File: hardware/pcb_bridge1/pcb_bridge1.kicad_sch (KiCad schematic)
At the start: 1 part, among them J1 TSM-103-01-L-DH

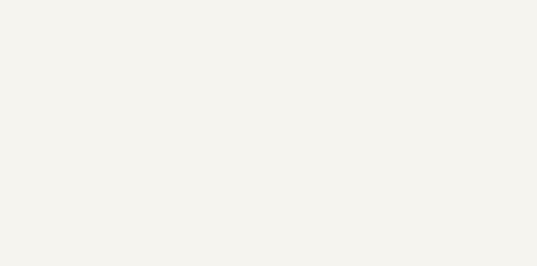
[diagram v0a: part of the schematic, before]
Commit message: Battery, zif added
nrf test points reduced
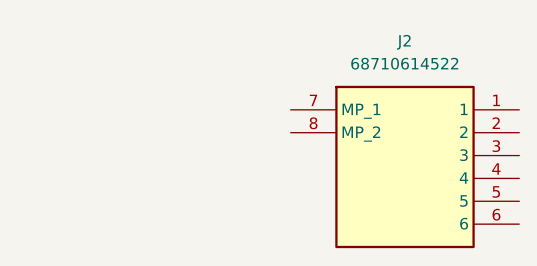
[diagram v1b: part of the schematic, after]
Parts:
- added J2: 68710614522, foots:68710614522, symbol 68710614522:68710614522
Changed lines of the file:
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@@
 	(paper "A4")
+	(symbol
+		(lib_id "68710614522:68710614522")
+		(at 128.27 43.18 0)
+		(unit 1)
+		(exclude_from_sim no)
+		(in_bom yes)
+		(on_board yes)
+		(dnp no)
+		(fields_autoplaced yes)
+		(property "Reference" "J2"
+			(at 140.97 35.56 0)
+			(effects
+				(font
+					(size 1.27 1.27)
+				)
+			)
+		)
+		(property "Value" "68710614522"
+			(at 140.97 38.1 0)
+			(effects
+				(font
+					(size 1.27 1.27)
+				)
+			)
+		)
+		(property "Footprint" "foots:68710614522"
+			(at 149.86 138.1 0)
+			(effects
+				(font
+					(size 1.27 1.27)
+				)
+				(justify left top)
+				(hide yes)
+			)
+		)
+		(property "Datasheet" ""
+			(at 149.86 238.1 0)
+			(effects
+				(font
+					(size 1.27 1.27)
+				)
+				(justify left top)
+				(hide yes)
+			)
+		)
+		(property "Description" "25WR-FPC 0.5mm ZIF Connector Bottom 6pin Wurth Elektronik 687 Series 0.5mm 6 Way 1 Row Straight PCB Socket Surface Mount Wire to Board"
+			(at 128.27 43.18 0)
+			(effects
+				(font
+					(size 1.27 1.27)
+				)
+				(hide yes)
+			)
+		)
+		(property "Height" "2.25"
+			(at 149.86 438.1 0)
+			(effects
+				(font
+					(size 1.27 1.27)
+				)
+				(justify left top)
+				(hide yes)
+			)
+		)
+		(property "Mouser Part Number" "710-68710614522"
+			(at 149.86 538.1 0)
+			(effects
+				(font
+					(size 1.27 1.27)
+				)
+				(justify left top)
+				(hide yes)
+			)
+		)
+		(property "Mouser Price/Stock" "https://www.mouser.co.uk/ProductDetail/Wurth-Elektronik/68710614522?qs=ZtY9WdtwX56jW0fVCAMn0A%3D%3D"
+			(at 149.86 638.1 0)
+			(effects
+				(font
+					(size 1.27 1.27)
+				)
+				(justify left top)
+				(hide yes)
+			)
+		)
+		(property "Manufacturer_Name" "Wurth Elektronik"
+			(at 149.86 738.1 0)
+			(effects
+				(font
+					(size 1.27 1.27)
+				)
+				(justify left top)
+				(hide yes)
+			)
+		)
+		(property "Manufacturer_Part_Number" "68710614522"
+			(at 149.86 838.1 0)
+			(effects
+				(font
+					(size 1.27 1.27)
+				)
+				(justify left top)
+				(hide yes)
+			)
+		)
+		(property "Distributor Link" "https://www.mouser.co.uk/ProductDetail/Wurth-Elektronik/68710614522?qs=ZtY9WdtwX56jW0fVCAMn0A%3D%3D"
+			(at 128.27 43.18 0)
+			(effects
+				(font
+					(size 1.27 1.27)
+				)
+				(hide yes)
+			)
+		)
+		(property "Manufacturer" "Wurth Elektronik"
+			(at 128.27 43.18 0)
+			(effects
+				(font
+					(size 1.27 1.27)
+				)
+				(hide yes)
+			)
+		)
+		(property "Manufacturer Part Number" "68710614522"
+			(at 128.27 43.18 0)
+			(effects
+				(font
+					(size 1.27 1.27)
+				)
+				(hide yes)
+			)
+		)
+		(pin "7"
+		)
+		(pin "8"
+		)
+		(pin "1"
+		)
+		(pin "2"
+		)
+		(pin "3"
+		)
+		(pin "4"
+		)
+		(pin "5"
+		)
+		(pin "6"
+		)
+		(instances
+			(project ""
+				(path "/0e6aa891-c6f8-4195-a67a-75cdb0397e25"
+					(reference "J2")
+					(unit 1)
+				)
+			)
+		)
+	)
 	(symbol
 		(lib_id "TSM-103-01-L-DH:TSM-103-01-L-DH")

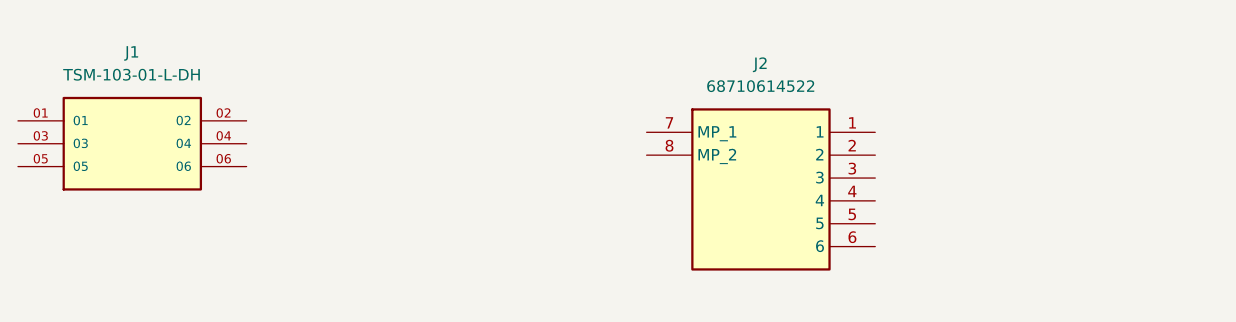
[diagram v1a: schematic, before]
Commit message: Bridges done, main layout done
layer pours done
CHanged zif connector to 8 wide to the bridge
Changed voltage levels
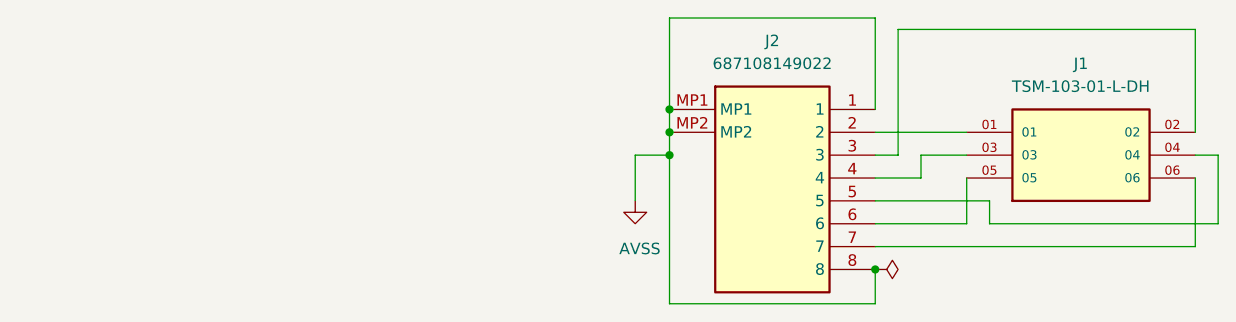
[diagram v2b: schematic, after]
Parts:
- removed J2: 68710614522, foots:68710614522, symbol 68710614522:68710614522
- added J2: 687108149022, foots:687108149022, symbol 687108149022:687108149022
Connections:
- net at J1.01: now also J2.2
- net at J1.02: now also J2.3
- net at J1.03: now also J2.4
- net at J1.04: now also J2.5
- net at J1.05: now also J2.6
- net at J1.06: now also J2.7
- new net AVSS: J2.1, J2.8, J2.MP1, J2.MP2
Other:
- moved on the sheet: J1
